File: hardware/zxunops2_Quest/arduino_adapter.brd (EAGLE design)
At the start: 37.6 x 38.3 mm, 8 parts

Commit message: Finalizo placa parte arduino
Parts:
- JP4, JP5: value M12PTH -> (none)
- MOUSE, ZXUNO: value DINC_MIN_TM_6_1 -> (none)
- moved JP6 0.16 mm to (24.3, 35.2)
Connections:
- removed net D7: JP4.3
- removed net D8: JP4.2
- removed net M1+: JP4.4
- removed net M1-: JP4.5
- removed net M2+: JP5.12
- removed net M2-: JP5.11
- removed net MISO: JP5.10
- removed net N$10: JP11.5
- removed net N$6: JP11.1
- removed net N$7: JP11.2
- removed net N$8: JP11.3
- removed net N$9: JP11.4
- removed net PB1: JP4.1
- removed net SCK: JP5.9
- removed net SEN1: JP6.1
- removed net SEN10: JP6.14
- removed net SEN3: JP6.7
- removed net SEN4: JP5.8, JP6.9
- removed net SEN5: JP4.8, JP6.11
- removed net SEN6: JP6.4
- removed net SEN7: JP6.6
- removed net SEN8: JP4.6, JP6.10
- removed net SW1: JP5.7
- new net A10: JP4.7, JP6.2
- new net A11: JP4.8, JP6.1
- new net A12: JP4.5, JP6.4
- new net A13: JP4.4, JP6.5
- new net A14: JP4.2, JP6.7
- new net A15: JP4.1, JP6.8
- new net A8: JP4.3, JP6.6
- new net A9: JP4.6, JP6.3
- new net D0: JP11.1, JP5.7
- new net D1: JP11.2, JP5.8
- new net D2: JP11.3, JP5.10
- new net D4: JP11.5, JP5.12
- net 3.3V: no longer JP6.5
- net D3: now also JP11.4, JP5.11; no longer JP4.7
- net GND: now also MOUSE.3; no longer JP6.13, JP6.2, JP6.8
- net VCC: now also MOUSE.4
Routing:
- net GND: track 0.00 -> 45.7 mm
- net PS2_CLK: track 0.00 -> 35.5 mm
- net PS2_DATA: track 0.00 -> 30.8 mm
- net D0: track 0.00 -> 27.0 mm
- net A15: track 0.00 -> 24.3 mm
- net D1: track 0.00 -> 23.4 mm
- net A8: track 0.00 -> 23.2 mm
- net N$3: track 0.00 -> 22.4 mm
- net A12: track 0.00 -> 22.2 mm
- net A10: track 0.00 -> 22.2 mm
- net A14: track 0.00 -> 20.7 mm
- net A11: track 0.00 -> 19.7 mm
- net A9: track 0.00 -> 19.6 mm
- net A13: track 0.00 -> 19.6 mm
- net D2: track 0.00 -> 19.1 mm
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
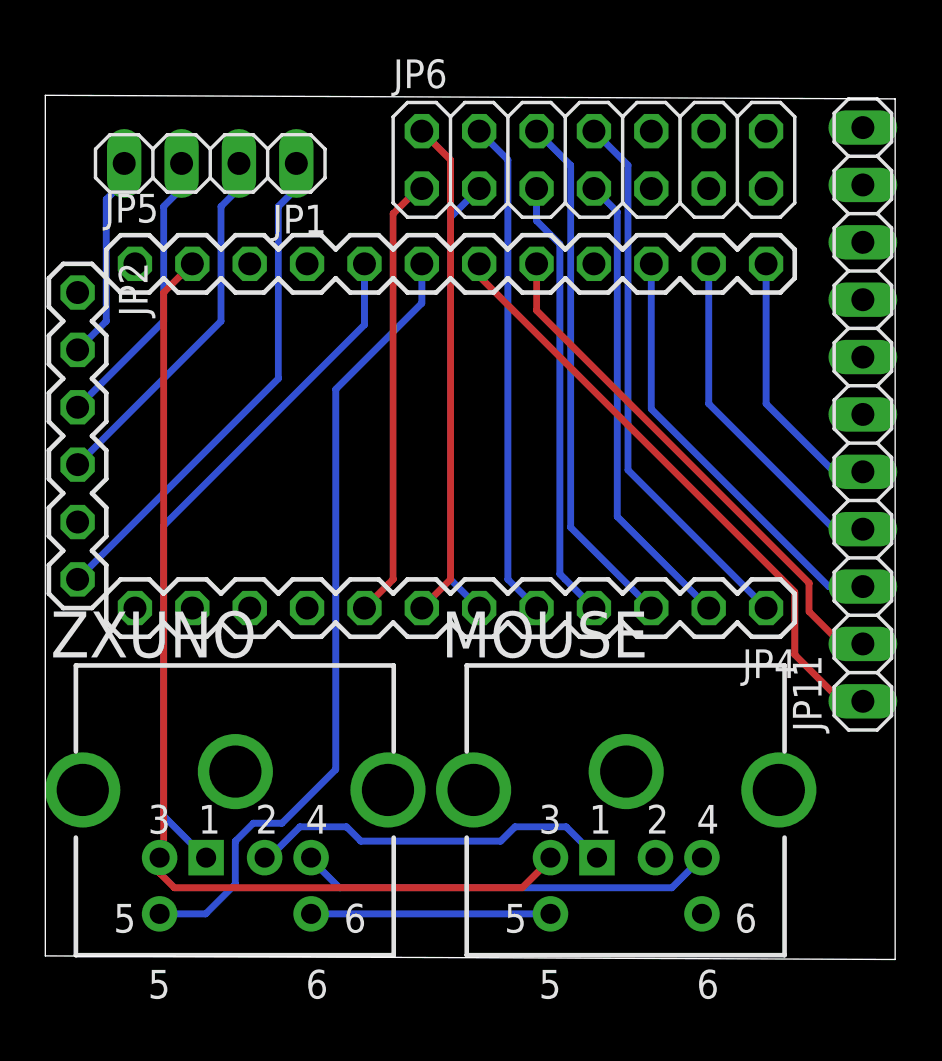
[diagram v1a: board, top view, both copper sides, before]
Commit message: 
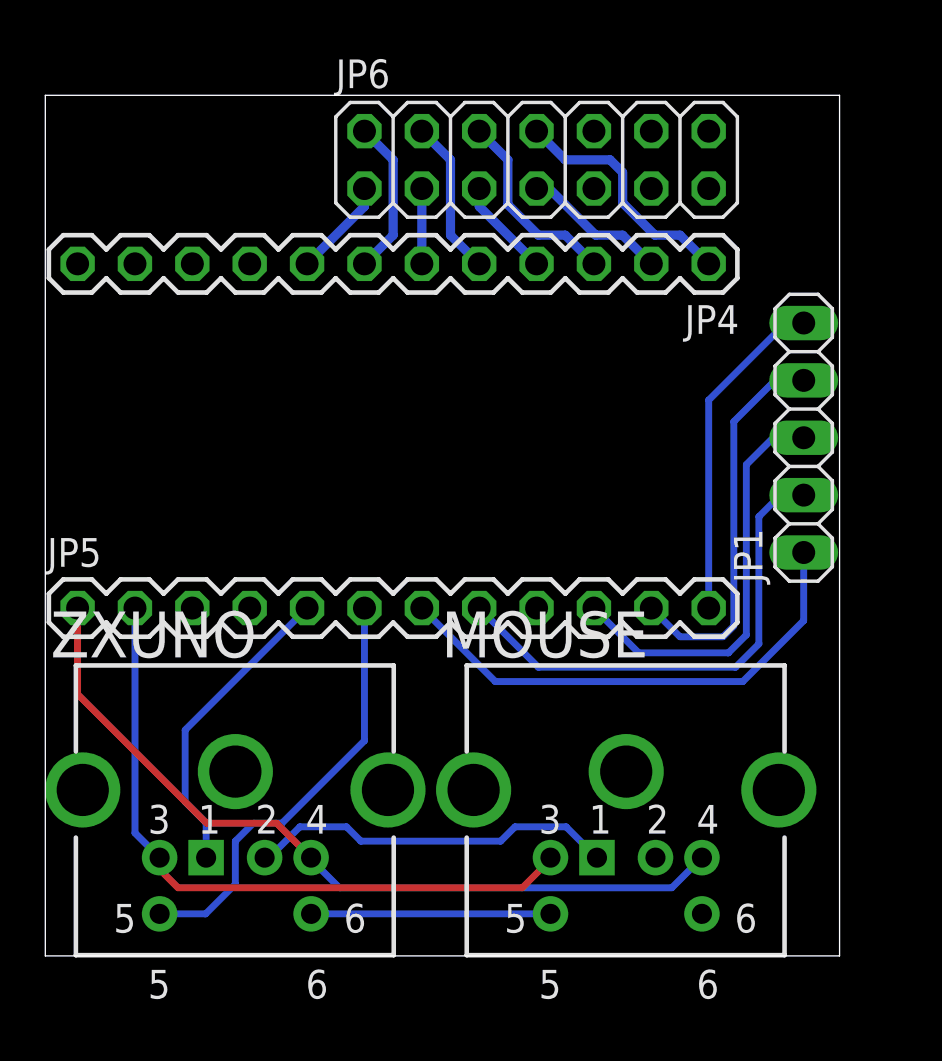
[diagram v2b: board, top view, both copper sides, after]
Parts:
- removed JP11: (no value), pinhead:1X11
- removed JP2: (no value), SparkFun-Connectors:1X06
- JP1: device pinhead:1X04 -> pinhead:1X05
- moved JP1 28.9 mm to (33.6, 22.9), turned to 90 degrees
- moved JP4 15.5 mm to (29.4, 30.6)
- moved JP5 15.5 mm to (1.43, 15.4)
- moved JP6 2.54 mm to (21.7, 35.2)
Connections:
- removed net 3.3V: JP5.4
- removed net 5V: JP5.1
- removed net N$3: JP1.1, JP2.GND
- removed net N$4: JP1.2, JP2.VCC
- removed net N$5: JP1.3, JP2.TXO
- removed net TXO: JP1.4, JP2.RXI
- net D0: now also JP1.1; no longer JP11.1
- net D1: now also JP1.2; no longer JP11.2
- net D2: now also JP1.3; no longer JP11.3
- net D3: now also JP1.4; no longer JP11.4
- net D4: now also JP1.5; no longer JP11.5
- net VCC: now also JP5.1
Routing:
- net N$3: track 22.4 -> 0.00 mm
- net VCC: track 18.5 -> 35.6 mm
- net PS2_DATA: track 30.8 -> 13.7 mm
- net N$4: track 16.3 -> 0.00 mm
- net PS2_CLK: track 35.5 -> 19.2 mm
- net A9: track 19.6 -> 3.33 mm
- net GND: track 45.7 -> 30.3 mm
- net A11: track 19.7 -> 4.39 mm
- net A12: track 22.2 -> 6.93 mm
- net A10: track 22.2 -> 6.93 mm
- net A13: track 19.6 -> 4.39 mm
- net A8: track 23.2 -> 8.68 mm
- net A14: track 20.7 -> 6.46 mm
- net A15: track 24.3 -> 10.8 mm
- net N$5: track 12.7 -> 0.00 mm
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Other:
- board size 37.6 x 38.3 mm -> 35.2 x 38.1 mm

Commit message: Añado proyecto buttom como referencia
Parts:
- removed JP1: (no value), pinhead:1X05
- added JP2: (no value), pinhead:1X11
- added U1: STM32F105RBT6, iwasz-logo:QFP50P1200X1200X160-64N
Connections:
- new net VBAT: U1.1
- new net VDDA: U1.13
- new net VDD_1: U1.32
- new net VDD_2: U1.48
- new net VDD_3: U1.64
- new net VDD_4: U1.19
- new net VSSA: U1.12
- new net VSS_1: U1.31
- new net VSS_2: U1.47
- new net VSS_3: U1.63
- new net VSS_4: U1.18
- net D0: now also JP2.1; no longer JP1.1
- net D1: now also JP2.2; no longer JP1.2
- net D2: now also JP2.3; no longer JP1.3
- net D3: now also JP2.4; no longer JP1.4
- net D4: now also JP2.5; no longer JP1.5
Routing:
- net D2: track 18.5 -> 11.4 mm
- net D4: track 14.8 -> 7.93 mm
- net D3: track 17.3 -> 10.4 mm
- net D1: track 21.9 -> 15.9 mm
- net D0: track 22.4 -> 18.6 mm
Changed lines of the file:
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@@
 <layer number="56" name="wert" color="7" fill="1" visible="no" active="no"/>
 <layer number="57" name="tCAD" color="7" fill="1" visible="no" active="no"/>
+<layer number="58" name="bCAD" color="7" fill="1" visible="yes" active="yes"/>
 <layer number="90" name="Modules" color="7" fill="1" visible="no" active="no"/>
 <layer number="91" name="Nets" color="2" fill="1" visible="no" active="no"/>
@@
 <attribute name="NAME" x="17.5387" y="13.21435" size="2.032" layer="25" font="vector" ratio="13" rot="SR0"/>
 </element>
-<element name="JP1" library="pinhead" package="1X05" value="" x="33.575625" y="22.939375" rot="R90"/>
+<element name="U1" library="iwasz-logo" package="QFP50P1200X1200X160-64N" value="STM32F105RBT6" x="20.081875" y="23.098125">
+<attribute name="PACKAGE" value="LQFP-64" x="20.081875" y="23.098125" size="1.778" layer="27" display="off"/>
+<attribute name="OC_FARNELL" value="1737133" x="20.081875" y="23.098125" size="1.778" layer="27" display="off"/>
+<attribute name="OC_NEWARK" value="25R9437" x="20.081875" y="23.098125" size="1.778" layer="27" display="off"/>
+<attribute name="SUPPLIER" value="STMicroelectronics" x="20.081875" y="23.098125" size="1.778" layer="27" display="off"/>
+<attribute name="MPN" value="STM32F105RBT6" x="20.081875" y="23.098125" size="1.778" layer="27" display="off"/>
+</element>
+<element name="JP2" library="pinhead" package="1X11" value="" x="33.575625" y="24.13" rot="R90"/>
 </elements>
 <signals>
@@
 <signal name="D3">
 <contactref element="JP5" pad="11"/>
-<contactref element="JP1" pad="4"/>
-<wire x1="30.48" y1="23.65375" x2="30.48" y2="14.605" width="0.3048" layer="16"/>
 <wire x1="30.48" y1="14.605" x2="30.00375" y2="14.12875" width="0.3048" layer="16"/>
 <wire x1="30.00375" y1="14.12875" x2="28.09875" y2="14.12875" width="0.3048" layer="16"/>
 <wire x1="28.09875" y1="14.12875" x2="26.82875" y2="15.39875" width="0.3048" layer="16"/>
-<wire x1="33.575625" y1="25.479375" x2="32.305625" y2="25.479375" width="0.3048" layer="16"/>
-<wire x1="32.305625" y1="25.479375" x2="30.48" y2="23.65375" width="0.3048" layer="16"/>
+<contactref element="JP2" pad="4"/>
+<wire x1="30.48" y1="14.605" x2="30.48" y2="16.430625" width="0.3048" layer="16"/>
+<wire x1="30.48" y1="16.430625" x2="33.099375" y2="19.05" width="0.3048" layer="16"/>
+<wire x1="33.575625" y1="19.05" x2="33.099375" y2="19.05" width="0.3048" layer="16"/>
 </signal>
 <signal name="A13">
@@
 <signal name="D0">
 <contactref element="JP5" pad="7"/>
-<contactref element="JP1" pad="1"/>
-<wire x1="33.575625" y1="17.859375" x2="33.575625" y2="14.843125" width="0.3048" layer="16"/>
-<wire x1="33.575625" y1="14.843125" x2="30.876875" y2="12.144375" width="0.3048" layer="16"/>
-<wire x1="30.876875" y1="12.144375" x2="19.923125" y2="12.144375" width="0.3048" layer="16"/>
+<wire x1="31.511875" y1="12.144375" x2="19.923125" y2="12.144375" width="0.3048" layer="16"/>
 <wire x1="19.923125" y1="12.144375" x2="16.66875" y2="15.39875" width="0.3048" layer="16"/>
+<contactref element="JP2" pad="1"/>
+<wire x1="31.511875" y1="12.144375" x2="32.146875" y2="11.509375" width="0.3048" layer="16"/>
+<wire x1="32.146875" y1="11.509375" x2="33.49625" y2="11.509375" width="0.3048" layer="16"/>
+<wire x1="33.49625" y1="11.509375" x2="33.575625" y2="11.43" width="0.3048" layer="16"/>
 </signal>
 <signal name="D1">
 <contactref element="JP5" pad="8"/>
-<contactref element="JP1" pad="2"/>
-<wire x1="33.575625" y1="20.399375" x2="32.54375" y2="20.399375" width="0.3048" layer="16"/>
-<wire x1="32.54375" y1="20.399375" x2="31.59125" y2="19.446875" width="0.3048" layer="16"/>
-<wire x1="31.59125" y1="19.446875" x2="31.59125" y2="13.81125" width="0.3048" layer="16"/>
-<wire x1="31.59125" y1="13.81125" x2="30.559375" y2="12.779375" width="0.3048" layer="16"/>
-<wire x1="30.559375" y1="12.779375" x2="21.828125" y2="12.779375" width="0.3048" layer="16"/>
+<wire x1="30.95625" y1="12.779375" x2="21.828125" y2="12.779375" width="0.3048" layer="16"/>
 <wire x1="21.828125" y1="12.779375" x2="19.20875" y2="15.39875" width="0.3048" layer="16"/>
+<contactref element="JP2" pad="2"/>
+<wire x1="30.95625" y1="12.779375" x2="32.146875" y2="13.97" width="0.3048" layer="16"/>
+<wire x1="32.146875" y1="13.97" x2="33.575625" y2="13.97" width="0.3048" layer="16"/>
 </signal>
 <signal name="D2">
 <contactref element="JP5" pad="10"/>
-<contactref element="JP1" pad="3"/>
-<wire x1="31.035625" y1="21.74875" x2="31.035625" y2="14.208125" width="0.3048" layer="16"/>
-<wire x1="31.035625" y1="14.208125" x2="30.241875" y2="13.414375" width="0.3048" layer="16"/>
 <wire x1="30.241875" y1="13.414375" x2="26.273125" y2="13.414375" width="0.3048" layer="16"/>
 <wire x1="26.273125" y1="13.414375" x2="24.28875" y2="15.39875" width="0.3048" layer="16"/>
-<wire x1="33.575625" y1="22.939375" x2="32.22625" y2="22.939375" width="0.3048" layer="16"/>
-<wire x1="32.22625" y1="22.939375" x2="31.035625" y2="21.74875" width="0.3048" layer="16"/>
+<contactref element="JP2" pad="3"/>
+<wire x1="30.241875" y1="13.414375" x2="33.3375" y2="16.51" width="0.3048" layer="16"/>
+<wire x1="33.575625" y1="16.51" x2="33.3375" y2="16.51" width="0.3048" layer="16"/>
 </signal>
 <signal name="D4">
 <contactref element="JP5" pad="12"/>
-<contactref element="JP1" pad="5"/>
-<wire x1="33.575625" y1="28.019375" x2="32.781875" y2="28.019375" width="0.3048" layer="16"/>
-<wire x1="32.781875" y1="28.019375" x2="29.36875" y2="24.60625" width="0.3048" layer="16"/>
-<wire x1="29.36875" y1="24.60625" x2="29.36875" y2="15.39875" width="0.3048" layer="16"/>
+<contactref element="JP2" pad="5"/>
+<wire x1="29.36875" y1="15.39875" x2="29.36875" y2="17.383125" width="0.3048" layer="16"/>
+<wire x1="29.36875" y1="17.383125" x2="33.575625" y2="21.59" width="0.3048" layer="16"/>
 </signal>
 <signal name="A11">
@@
 <wire x1="16.66875" y1="33.9725" x2="16.66875" y2="30.63875" width="0.4064" layer="16"/>
 </signal>
+<signal name="VBAT">
+<contactref element="U1" pad="1"/>
+</signal>
+<signal name="VDDA">
+<contactref element="U1" pad="13"/>
+</signal>
+<signal name="VDD_1">
+<contactref element="U1" pad="32"/>
+</signal>
+<signal name="VDD_2">
+<contactref element="U1" pad="48"/>
+</signal>
+<signal name="VDD_3">
+<contactref element="U1" pad="64"/>
+</signal>
+<signal name="VDD_4">
+<contactref element="U1" pad="19"/>
+</signal>
+<signal name="VSSA">
+<contactref element="U1" pad="12"/>
+</signal>
+<signal name="VSS_1">
+<contactref element="U1" pad="31"/>
+</signal>
+<signal name="VSS_2">
+<contactref element="U1" pad="47"/>
+</signal>
+<signal name="VSS_3">
+<contactref element="U1" pad="63"/>
+</signal>
+<signal name="VSS_4">
+<contactref element="U1" pad="18"/>
+</signal>
 </signals>

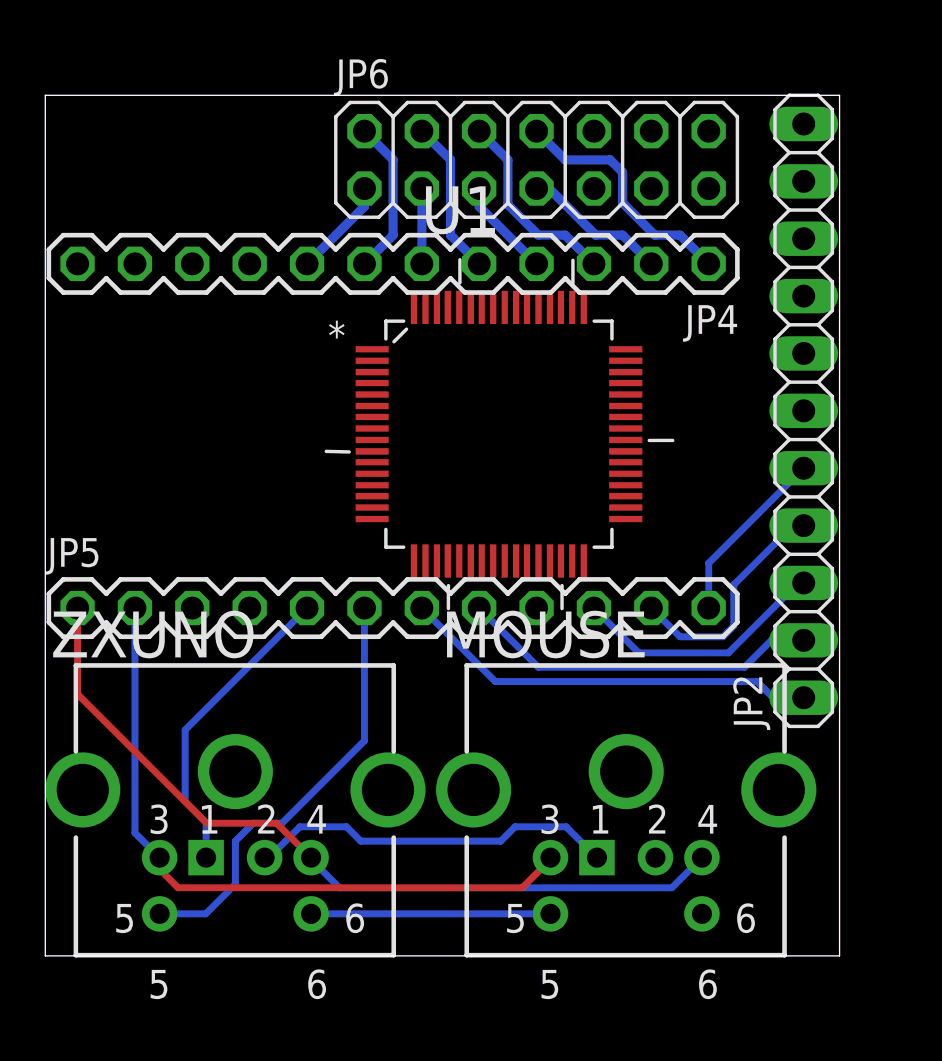
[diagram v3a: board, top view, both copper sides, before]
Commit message: Junto conector PS/2 ratón para que no choque con conector de faja
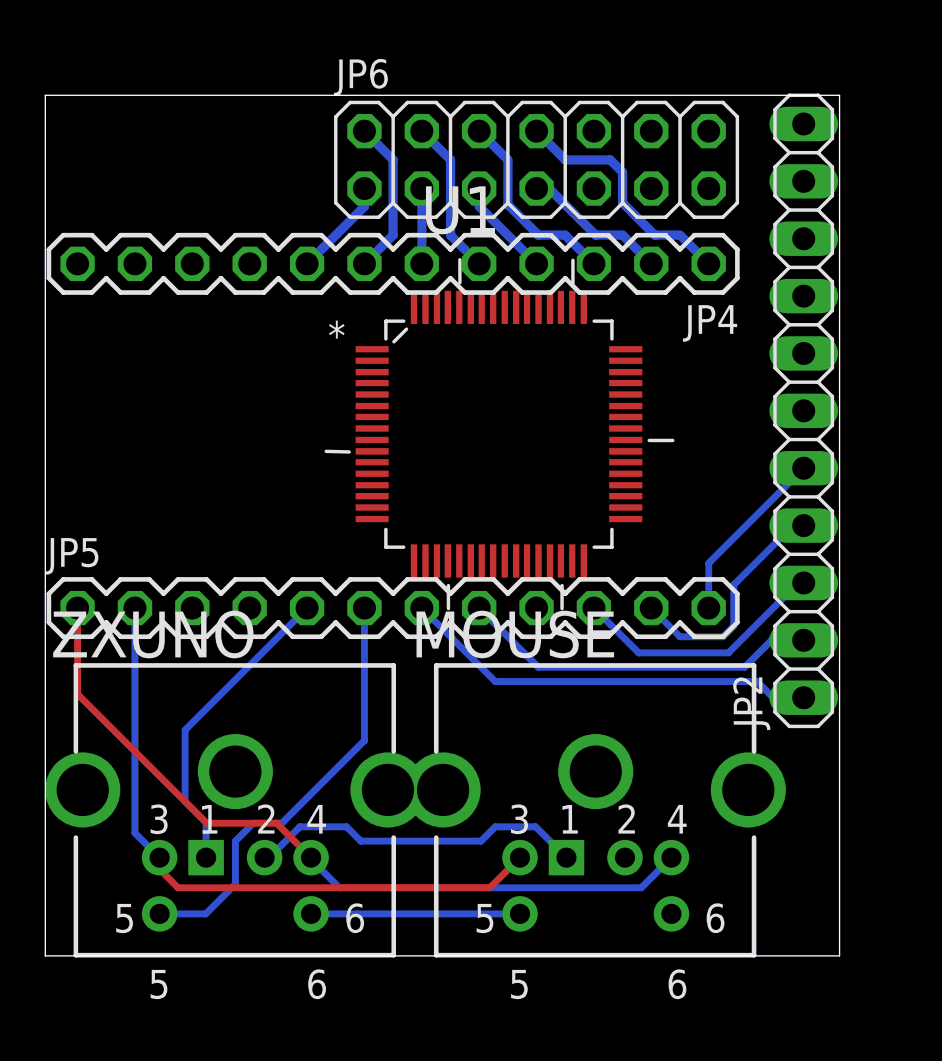
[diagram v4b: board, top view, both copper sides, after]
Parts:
- moved MOUSE 1.35 mm to (24.4, 12.9)
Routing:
- net GND: track 30.3 -> 28.9 mm
- net N$2: track 16.4 -> 15.0 mm
- net N$1: track 10.6 -> 9.25 mm
- net VCC: track 35.6 -> 34.3 mm
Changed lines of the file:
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@@
 <attribute name="NAME" x="0.23495" y="13.21435" size="2.032" layer="25" font="vector" ratio="13" rot="SR0"/>
 </element>
-<element name="MOUSE" library="ZX_UNO_0_14" package="DINC/MIN_TM/6_1PRIMARY" value="" x="25.7175" y="12.85875" smashed="yes">
-<attribute name="NAME" x="17.5387" y="13.21435" size="2.032" layer="25" font="vector" ratio="13" rot="SR0"/>
+<element name="MOUSE" library="ZX_UNO_0_14" package="DINC/MIN_TM/6_1PRIMARY" value="" x="24.368125" y="12.85875" smashed="yes">
+<attribute name="NAME" x="16.189325" y="13.21435" size="2.032" layer="25" font="vector" ratio="13" rot="SR0"/>
 </element>
 <element name="U1" library="iwasz-logo" package="QFP50P1200X1200X160-64N" value="STM32F105RBT6" x="20.081875" y="23.098125">
@@
 <contactref element="ZXUNO" pad="3"/>
 <contactref element="MOUSE" pad="3"/>
-<wire x1="22.3647" y1="4.34975" x2="22.3647" y2="4.2672" width="0.3048" layer="1"/>
-<wire x1="22.3647" y1="4.2672" x2="21.11375" y2="3.01625" width="0.3048" layer="1"/>
-<wire x1="21.11375" y1="3.01625" x2="5.87375" y2="3.01625" width="0.3048" layer="1"/>
 <wire x1="3.96875" y1="15.478125" x2="3.96875" y2="15.39875" width="0.3048" layer="16"/>
 <wire x1="3.96875" y1="15.39875" x2="3.96875" y2="5.44195" width="0.3048" layer="16"/>
@@
 <wire x1="5.87375" y1="3.01625" x2="5.08" y2="3.81" width="0.3048" layer="1"/>
 <wire x1="5.08" y1="4.3307" x2="5.08" y2="3.81" width="0.3048" layer="1"/>
+<wire x1="5.87375" y1="3.01625" x2="19.681825" y2="3.01625" width="0.3048" layer="1"/>
+<wire x1="19.681825" y1="3.01625" x2="21.015325" y2="4.34975" width="0.3048" layer="1"/>
 <wire x1="5.06095" y1="4.34975" x2="5.08" y2="4.3307" width="0" layer="19" extent="1-1"/>
 </signal>
@@
 <contactref element="ZXUNO" pad="6"/>
 <contactref element="MOUSE" pad="5"/>
-<wire x1="11.76655" y1="1.86055" x2="22.3647" y2="1.86055" width="0.3048" layer="16"/>
+<wire x1="11.76655" y1="1.86055" x2="21.015325" y2="1.86055" width="0.3048" layer="16"/>
 </signal>
 <signal name="N$2">
@@
 <wire x1="11.27125" y1="5.715" x2="13.335" y2="5.715" width="0.3048" layer="16"/>
 <wire x1="13.335" y1="5.715" x2="13.97" y2="5.08" width="0.3048" layer="16"/>
-<wire x1="13.97" y1="5.08" x2="20.16125" y2="5.08" width="0.3048" layer="16"/>
-<wire x1="20.16125" y1="5.08" x2="20.79625" y2="5.715" width="0.3048" layer="16"/>
-<wire x1="20.79625" y1="5.715" x2="23.05685" y2="5.715" width="0.3048" layer="16"/>
-<wire x1="23.05685" y1="5.715" x2="24.4221" y2="4.34975" width="0.3048" layer="16"/>
+<wire x1="13.97" y1="5.08" x2="19.288125" y2="5.08" width="0.3048" layer="16"/>
+<wire x1="19.288125" y1="5.08" x2="19.923125" y2="5.715" width="0.3048" layer="16"/>
+<wire x1="19.923125" y1="5.715" x2="21.707475" y2="5.715" width="0.3048" layer="16"/>
+<wire x1="21.707475" y1="5.715" x2="23.072725" y2="4.34975" width="0.3048" layer="16"/>
 </signal>
 <signal name="VCC">
@@
 <wire x1="11.76655" y1="4.34975" x2="11.76655" y2="4.2672" width="0.3048" layer="16"/>
 <wire x1="11.76655" y1="4.2672" x2="13.0175" y2="3.01625" width="0.3048" layer="16"/>
-<wire x1="13.0175" y1="3.01625" x2="27.7368" y2="3.01625" width="0.3048" layer="16"/>
-<wire x1="27.7368" y1="3.01625" x2="29.0703" y2="4.34975" width="0.3048" layer="16"/>
 <contactref element="JP5" pad="1"/>
 <wire x1="7.14375" y1="5.87375" x2="10.24255" y2="5.87375" width="0.3048" layer="1"/>
@@
 <wire x1="7.14375" y1="5.87375" x2="1.42875" y2="11.58875" width="0.3048" layer="1"/>
 <wire x1="1.42875" y1="11.58875" x2="1.42875" y2="15.39875" width="0.3048" layer="1"/>
+<wire x1="13.0175" y1="3.01625" x2="26.387425" y2="3.01625" width="0.3048" layer="16"/>
+<wire x1="26.387425" y1="3.01625" x2="27.720925" y2="4.34975" width="0.3048" layer="16"/>
 </signal>
 <signal name="D0">
